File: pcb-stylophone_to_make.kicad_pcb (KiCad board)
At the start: 2 copper layers, 65 x 45 mm, 48 parts, among them J1 Batt, J10 Key 9, J11 Key 10, J12 Key 11, J13 Key 12, J14 Key 13, J15 Key 14, J16 Key 15, J17 Key 16, J18 Key 17, J19 Key 18, J2 Key 1, J20 Key 19, J21 Key 20, J22 Stylus, J3 Key 2, J4 Key 3, J5 Key 4, J6 Key 5, J7 Key 6, J8 Key 7, J9 Key 8, U1 NE555P

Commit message: finalised v1
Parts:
- removed J10: Key 9, TestPoint:TestPoint_Pad_1.0x1.0mm
- removed J11: Key 10, TestPoint:TestPoint_Pad_1.0x1.0mm
- removed J12: Key 11, TestPoint:TestPoint_Pad_1.0x1.0mm
- removed J13: Key 12, TestPoint:TestPoint_Pad_1.0x1.0mm
- removed J14: Key 13, TestPoint:TestPoint_Pad_1.0x1.0mm
- removed J15: Key 14, TestPoint:TestPoint_Pad_1.0x1.0mm
- removed J16: Key 15, TestPoint:TestPoint_Pad_1.0x1.0mm
- removed J17: Key 16, TestPoint:TestPoint_Pad_1.0x1.0mm
- removed J18: Key 17, TestPoint:TestPoint_Pad_1.0x1.0mm
- removed J19: Key 18, TestPoint:TestPoint_Pad_1.0x1.0mm
- removed J2: Key 1, TestPoint:TestPoint_Pad_1.0x1.0mm
- removed J20: Key 19, TestPoint:TestPoint_Pad_1.0x1.0mm
- removed J21: Key 20, TestPoint:TestPoint_Pad_1.0x1.0mm
- removed J3: Key 2, TestPoint:TestPoint_Pad_1.0x1.0mm
- removed J4: Key 3, TestPoint:TestPoint_Pad_1.0x1.0mm
- removed J5: Key 4, TestPoint:TestPoint_Pad_1.0x1.0mm
- removed J6: Key 5, TestPoint:TestPoint_Pad_1.0x1.0mm
- removed J7: Key 6, TestPoint:TestPoint_Pad_1.0x1.0mm
- removed J8: Key 7, TestPoint:TestPoint_Pad_1.0x1.0mm
- removed J9: Key 8, TestPoint:TestPoint_Pad_1.0x1.0mm

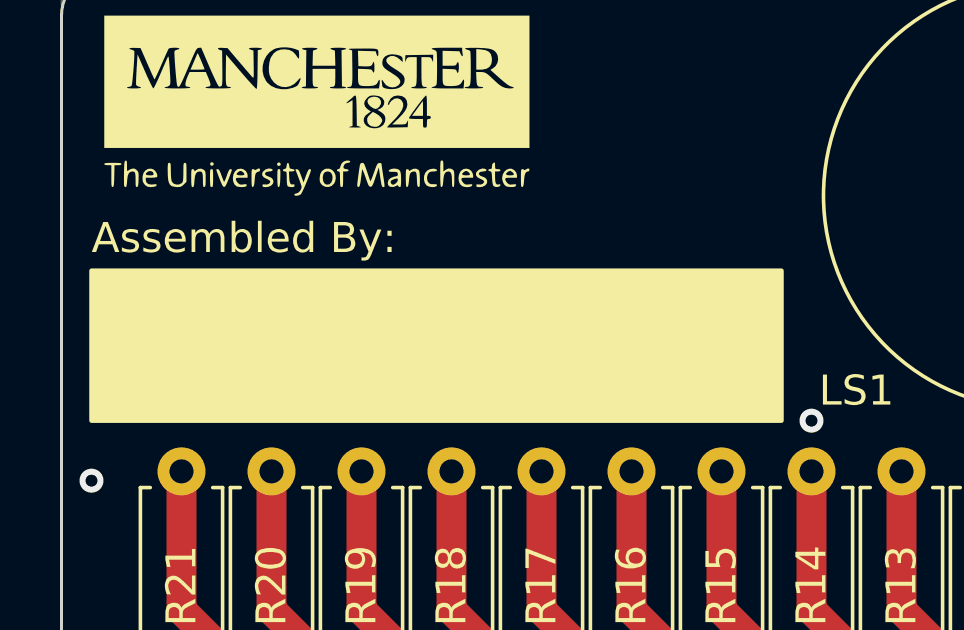
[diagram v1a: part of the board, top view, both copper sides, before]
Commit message: stylophone v2 has bigger resistor soldering pads
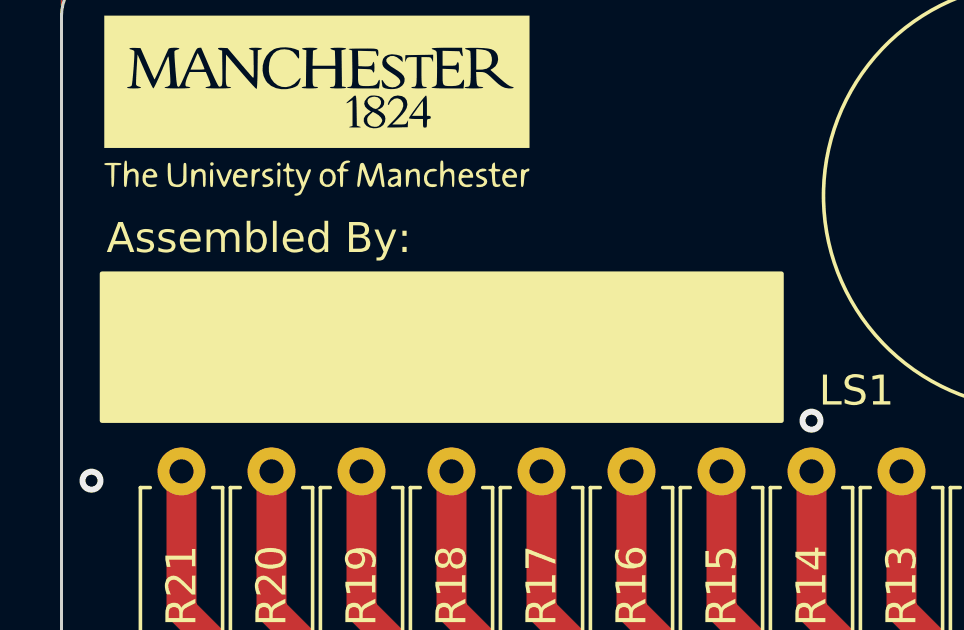
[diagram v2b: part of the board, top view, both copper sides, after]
